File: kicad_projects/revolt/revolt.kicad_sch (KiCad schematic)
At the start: 85 parts, among them J1 IDC-Header_2x07_P2.54mm_Verti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

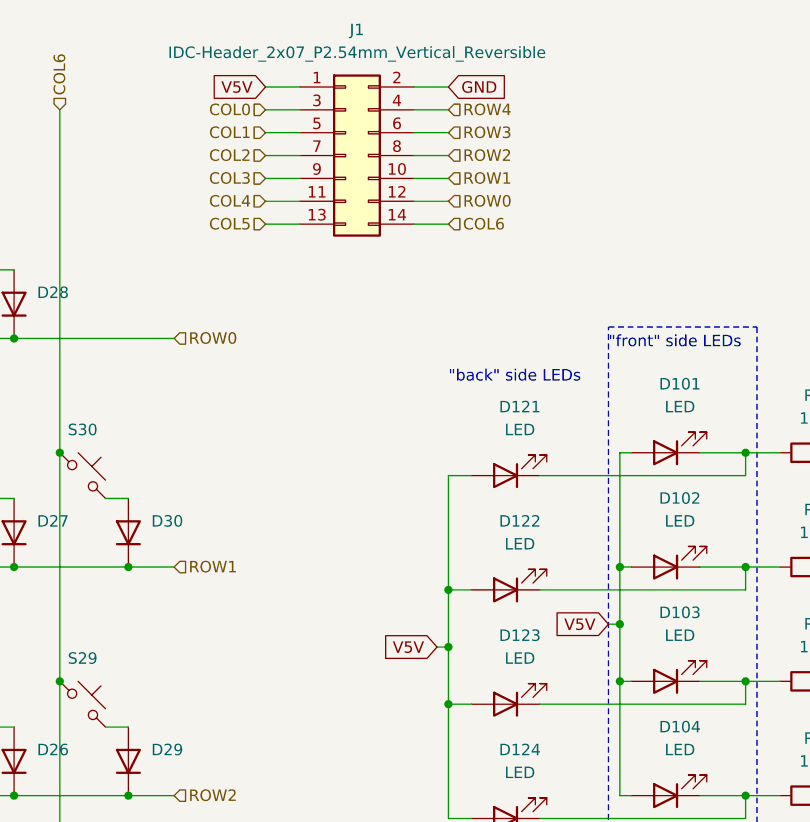
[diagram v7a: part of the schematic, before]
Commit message: Commander board passing DRC
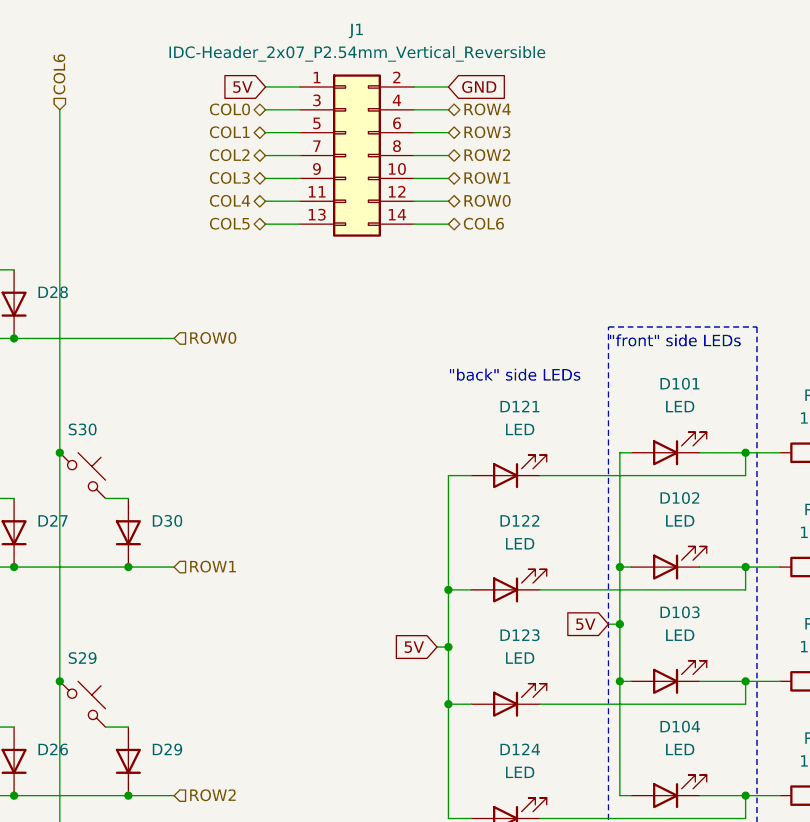
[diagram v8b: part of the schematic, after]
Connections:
- net V5V renamed 5V
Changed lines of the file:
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@@
     )
   )
-  (global_label "V5V" (shape input) (at 187.96 82.55 180) (fields_autoplaced)
+  (global_label "5V" (shape input) (at 187.96 82.55 180) (fields_autoplaced)
     (effects (font (size 1.27 1.27)) (justify right))
-    (property "Intersheetrefs" "${INTERSHEET_REFS}" (at 181.5881 82.55 0)
+    (property "Intersheetrefs" "${INTERSHEET_REFS}" (at 182.6767 82.55 0)
       (effects (font (size 1.27 1.27)) (justify right) hide)
     )
   )
-  (global_label "V5V" (shape input) (at 168.91 85.09 180) (fields_autoplaced)
+  (global_label "5V" (shape input) (at 168.91 85.09 180) (fields_autoplaced)
     (effects (font (size 1.27 1.27)) (justify right))
-    (property "Intersheetrefs" "${INTERSHEET_REFS}" (at 162.5381 85.09 0)
+    (property "Intersheetrefs" "${INTERSHEET_REFS}" (at 163.6267 85.09 0)
       (effects (font (size 1.27 1.27)) (justify right) hide)
     )
@@
     )
   )
-  (global_label "V5V" (shape input) (at 149.86 22.86 180) (fields_autoplaced)
+  (global_label "5V" (shape input) (at 149.86 22.86 180) (fields_autoplaced)
     (effects (font (size 1.27 1.27)) (justify right))
-    (property "Intersheetrefs" "${INTERSHEET_REFS}" (at 143.4881 22.86 0)
+    (property "Intersheetrefs" "${INTERSHEET_REFS}" (at 144.5767 22.86 0)
       (effects (font (size 1.27 1.27)) (justify right) hide)
     )
@@
     (effects (font (size 1.27 1.27)) (justify left))
   )
-  (hierarchical_label "COL5" (shape input) (at 149.86 38.1 180) (fields_autoplaced)
+  (hierarchical_label "COL5" (shape bidirectional) (at 149.86 38.1 180) (fields_autoplaced)
     (effects (font (size 1.27 1.27)) (justify right))
   )
@@
     (effects (font (size 1.27 1.27)) (justify left))
   )
-  (hierarchical_label "COL6" (shape input) (at 170.18 38.1 0) (fields_autoplaced)
+  (hierarchical_label "COL6" (shape bidirectional) (at 170.18 38.1 0) (fields_autoplaced)
     (effects (font (size 1.27 1.27)) (justify left))
   )
-  (hierarchical_label "ROW1" (shape input) (at 170.18 33.02 0) (fields_autoplaced)
+  (hierarchical_label "ROW1" (shape bidirectional) (at 170.18 33.02 0) (fields_autoplaced)
     (effects (font (size 1.27 1.27)) (justify left))
   )
@@
     (effects (font (size 1.27 1.27)) (justify left))
   )
-  (hierarchical_label "COL4" (shape input) (at 149.86 35.56 180) (fields_autoplaced)
+  (hierarchical_label "COL4" (shape bidirectional) (at 149.86 35.56 180) (fields_autoplaced)
     (effects (font (size 1.27 1.27)) (justify right))
   )
-  (hierarchical_label "ROW2" (shape input) (at 170.18 30.48 0) (fields_autoplaced)
+  (hierarchical_label "ROW2" (shape bidirectional) (at 170.18 30.48 0) (fields_autoplaced)
     (effects (font (size 1.27 1.27)) (justify left))
   )
-  (hierarchical_label "ROW3" (shape input) (at 170.18 27.94 0) (fields_autoplaced)
+  (hierarchical_label "ROW3" (shape bidirectional) (at 170.18 27.94 0) (fields_autoplaced)
     (effects (font (size 1.27 1.27)) (justify left))
   )
@@
     (effects (font (size 1.27 1.27)) (justify left))
   )
-  (hierarchical_label "COL0" (shape input) (at 149.86 25.4 180) (fields_autoplaced)
+  (hierarchical_label "COL0" (shape bidirectional) (at 149.86 25.4 180) (fields_autoplaced)
     (effects (font (size 1.27 1.27)) (justify right))
   )
@@
     (effects (font (size 1.27 1.27)) (justify left))
   )
-  (hierarchical_label "ROW4" (shape input) (at 170.18 25.4 0) (fields_autoplaced)
+  (hierarchical_label "ROW4" (shape bidirectional) (at 170.18 25.4 0) (fields_autoplaced)
     (effects (font (size 1.27 1.27)) (justify left))
   )
@@
     (effects (font (size 1.27 1.27)) (justify left))
   )
-  (hierarchical_label "COL3" (shape input) (at 149.86 33.02 180) (fields_autoplaced)
+  (hierarchical_label "COL3" (shape bidirectional) (at 149.86 33.02 180) (fields_autoplaced)
     (effects (font (size 1.27 1.27)) (justify right))
   )
-  (hierarchical_label "COL1" (shape input) (at 149.86 27.94 180) (fields_autoplaced)
+  (hierarchical_label "COL1" (shape bidirectional) (at 149.86 27.94 180) (fields_autoplaced)
     (effects (font (size 1.27 1.27)) (justify right))
   )
-  (hierarchical_label "ROW0" (shape input) (at 170.18 35.56 0) (fields_autoplaced)
+  (hierarchical_label "ROW0" (shape bidirectional) (at 170.18 35.56 0) (fields_autoplaced)
     (effects (font (size 1.27 1.27)) (justify left))
   )
-  (hierarchical_label "COL2" (shape input) (at 149.86 30.48 180) (fields_autoplaced)
+  (hierarchical_label "COL2" (shape bidirectional) (at 149.86 30.48 180) (fields_autoplaced)
     (effects (font (size 1.27 1.27)) (justify right))
   )
